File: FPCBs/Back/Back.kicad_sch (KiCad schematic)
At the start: 24 parts, among them J1 To PCB, J2 To Front, J3 Front, J4 EVF_SENSOR, J5 From LCD, SW1 MENU/SET, SW10 -+-, SW11 PLAY, SW12 BACK_WHEEL, SW13 S/C/M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

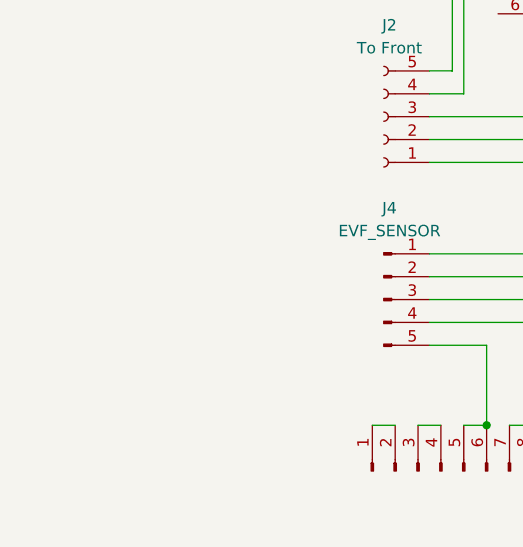
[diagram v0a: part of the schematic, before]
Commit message: Update the licence with CERN-OHL-P-2.0
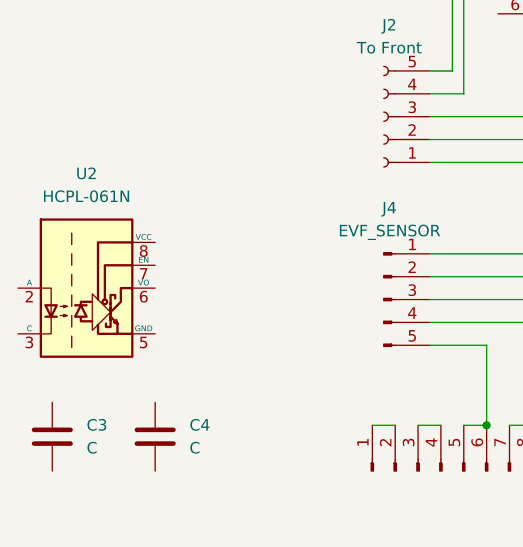
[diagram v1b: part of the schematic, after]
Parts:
- added C3, C4: C, Leica-G9ii:R_0603, symbol Device:C
- added U2: HCPL-061N, Package_SO:SOIC-8_3.9x4.9mm_P1.27mm, symbol Isolator:HCPL-061N
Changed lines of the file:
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@@
+	)
+	(symbol
+		(lib_id "Isolator:HCPL-061N")
+		(at 44.45 139.7 0)
+		(unit 1)
+		(exclude_from_sim no)
+		(in_bom yes)
+		(on_board yes)
+		(dnp no)
+		(fields_autoplaced yes)
+		(property "Reference" "U2"
+			(at 44.45 127 0)
+			(effects
+				(font
+					(size 1.27 1.27)
+				)
+			)
+		)
+		(property "Value" "HCPL-061N"
+			(at 44.45 129.54 0)
+			(effects
+				(font
+					(size 1.27 1.27)
+				)
+			)
+		)
+		(property "Footprint" "Package_SO:SOIC-8_3.9x4.9mm_P1.27mm"
+			(at 44.45 152.4 0)
+			(effects
+				(font
+					(size 1.27 1.27)
+				)
+				(hide yes)
+			)
+		)
+		(property "Datasheet" "http://docs.avagotech.com/docs/AV02-0391EN"
+			(at 22.86 124.46 0)
+			(effects
+				(font
+					(size 1.27 1.27)
+				)
+				(hide yes)
+			)
+		)
+		(property "Description" "Single High Speed HCMOS/LSTTL/TTL Compatible Optocoupler with enable, dV/dt 1000/us, VCM 1000, -0.5V to 7V VCC, SOIC-8"
+			(at 44.45 139.7 0)
+			(effects
+				(font
+					(size 1.27 1.27)
+				)
+				(hide yes)
+			)
+		)
+		(pin "5"
+		)
+		(pin "6"
+		)
+		(pin "8"
+		)
+		(pin "2"
+		)
+		(pin "3"
+		)
+		(pin "1"
+		)
+		(pin "7"
+		)
+		(instances
+			(project ""
+				(path "/2c10aa51-a3b8-43c6-b36e-0de96e4fe4d6"
+					(reference "U2")
+					(unit 1)
+				)
+			)
+		)
 	)
 	(symbol
@@
 	)
 	(symbol
+		(lib_id "Device:C")
+		(at 40.64 156.21 0)
+		(unit 1)
+		(exclude_from_sim no)
+		(in_bom yes)
+		(on_board yes)
+		(dnp no)
+		(fields_autoplaced yes)
+		(property "Reference" "C3"
+			(at 44.45 154.9399 0)
+			(effects
+				(font
+					(size 1.27 1.27)
+				)
+				(justify left)
+			)
+		)
+		(property "Value" "C"
+			(at 44.45 157.4799 0)
+			(effects
+				(font
+					(size 1.27 1.27)
+				)
+				(justify left)
+			)
+		)
+		(property "Footprint" "Leica-G9ii:R_0603"
+			(at 41.6052 160.02 0)
+			(effects
+				(font
+					(size 1.27 1.27)
+				)
+				(hide yes)
+			)
+		)
+		(property "Datasheet" "~"
+			(at 40.64 156.21 0)
+			(effects
+				(font
+					(size 1.27 1.27)
+				)
+				(hide yes)
+			)
+		)
+		(property "Description" "Unpolarized capacitor"
+			(at 40.64 156.21 0)
+			(effects
+				(font
+					(size 1.27 1.27)
+				)
+				(hide yes)
+			)
+		)
+		(pin "2"
+		)
+		(pin "1"
+		)
+		(instances
+			(project "Back"
+				(path "/2c10aa51-a3b8-43c6-b36e-0de96e4fe4d6"
+					(reference "C3")
+					(unit 1)
+				)
+			)
+		)
+	)
+	(symbol
 		(lib_id "Switch:SW_Push_Dual_x2")
 		(at 154.94 95.25 0)
@@
 					(unit 1)
 				)
+			)
+		)
+	)
+	(symbol
+		(lib_id "Device:C")
+		(at 52.07 156.21 0)
+		(unit 1)
+		(exclude_from_sim no)
+		(in_bom yes)
+		(on_board yes)
+		(dnp no)
+		(fields_autoplaced yes)
+		(property "Reference" "C4"
+			(at 55.88 154.9399 0)
+			(effects
+				(font
+					(size 1.27 1.27)
+				)
+				(justify left)
+			)
+		)
+		(property "Value" "C"
+			(at 55.88 157.4799 0)
+			(effects
+				(font
+					(size 1.27 1.27)
+				)
+				(justify left)
+			)
+		)
+		(property "Footprint" "Leica-G9ii:R_0603"
+			(at 53.0352 160.02 0)
+			(effects
+				(font
+					(size 1.27 1.27)
+				)
+				(hide yes)
+			)
+		)
+		(property "Datasheet" "~"
+			(at 52.07 156.21 0)
+			(effects
+				(font
+					(size 1.27 1.27)
+				)
+				(hide yes)
+			)
+		)
+		(property "Description" "Unpolarized capacitor"
+			(at 52.07 156.21 0)
+			(effects
+				(font
+					(size 1.27 1.27)
+				)
+				(hide yes)
+			)
+		)
+		(pin "2"
+		)
+		(pin "1"
+		)
+		(instances
+			(project "Back"
+				(path "/2c10aa51-a3b8-43c6-b36e-0de96e4fe4d6"
+					(reference "C4")
+					(unit 1)
+				)

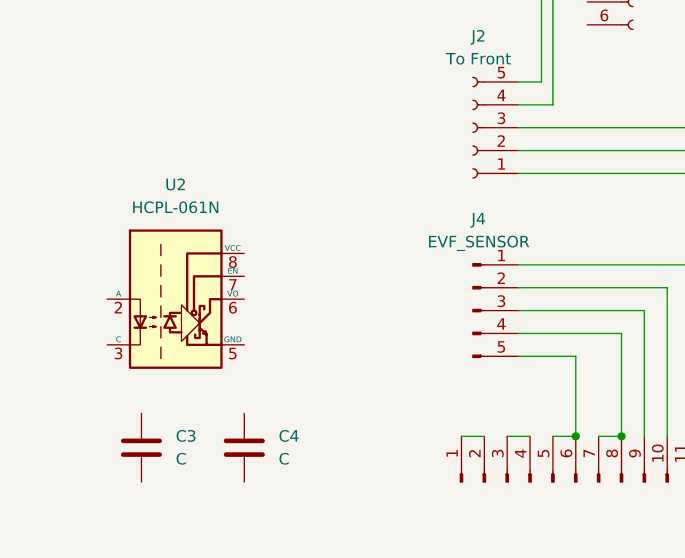
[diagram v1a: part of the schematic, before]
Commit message: Add EVF optocoupler
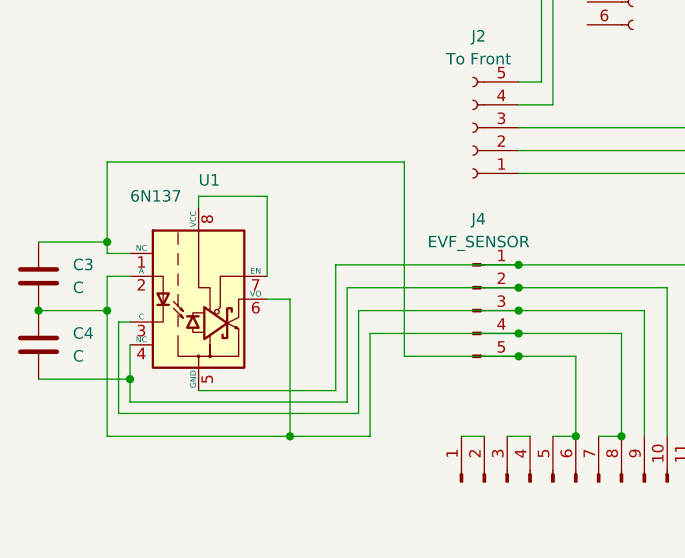
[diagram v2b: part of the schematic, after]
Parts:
- removed U2: HCPL-061N, Package_SO:SOIC-8_3.9x4.9mm_P1.27mm, symbol Isolator:HCPL-061N
- added U1: 6N137, Leica-G9ii:Optocoupler_EVF, symbol Isolator:6N137
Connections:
- net at C3.1: now also J1.5 (Pin_5), J1.6 (Pin_6), J4.5 (Pin_5), U1.1 (NC)
- net at C3.2: now also C4.1, J1.7 (Pin_7), J1.8 (Pin_8), J4.4 (Pin_4), U1.2 (A), U1.6 (VO)
- net at J1.10 (Pin_10), J4.2 (Pin_2): now also C4.2, U1.4 (NC)
- net at J1.11 (Pin_11), J4.1 (Pin_1): now also U1.5 (GND)
- net at J1.9 (Pin_9), J4.3 (Pin_3): now also U1.3 (C)
- new net: U1.7 (EN), U1.8 (VCC)
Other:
- moved on the sheet: C3, C4

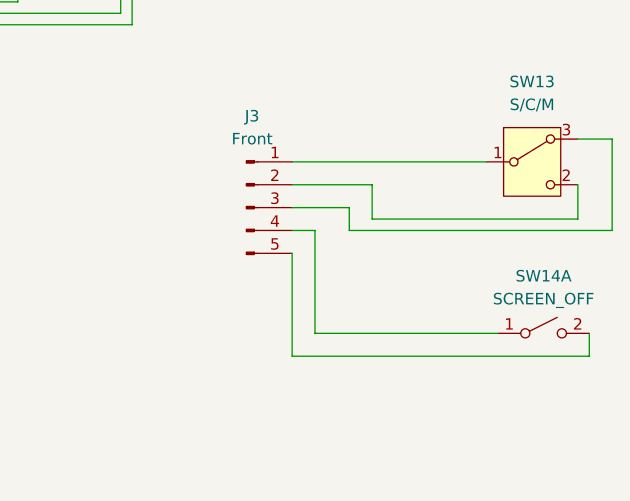
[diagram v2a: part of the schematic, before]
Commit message: Improve the back fpcb
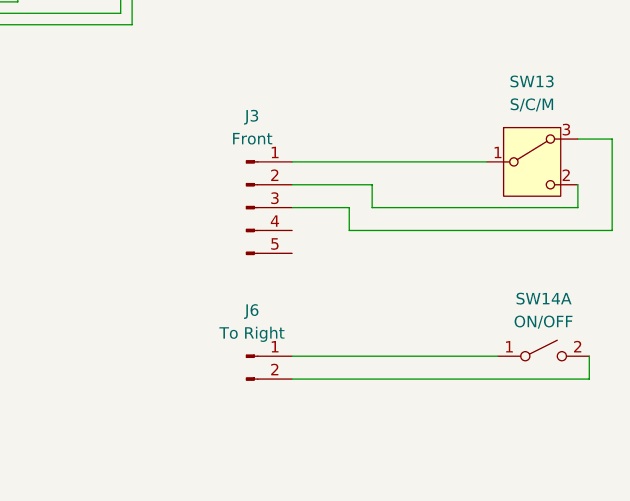
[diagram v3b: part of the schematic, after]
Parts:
- added J6: To Right, Leica-G9ii:Connector-Screw-2Pins, symbol Connector:Conn_01x02_Pin
- SW14: value SCREEN_OFF -> ON/OFF
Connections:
- net at SW14.1 (A): now also J6.1 (Pin_1); no longer J3.4 (Pin_4)
- net at SW14.2 (B): now also J6.2 (Pin_2); no longer J3.5 (Pin_5)
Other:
- moved on the sheet: SW14A
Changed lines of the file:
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@@
-	(wire
-		(pts
-			(xy 256.54 149.86) (xy 236.22 149.86)
-		)
-		(stroke
-			(width 0)
-			(type default)
-		)
-	)
 	(wire
 		(pts
@@
 	(wire
 		(pts
-			(xy 242.57 137.16) (xy 265.43 137.16)
+			(xy 242.57 135.89) (xy 265.43 135.89)
 		)
 		(stroke
@@
 	(wire
 		(pts
-			(xy 236.22 138.43) (xy 233.68 138.43)
-		)
-		(stroke
-			(width 0)
-			(type default)
-		)
-	)
-	(wire
-		(pts
 			(xy 81.28 154.94) (xy 83.82 154.94)
 		)
@@
 	(wire
 		(pts
-			(xy 233.68 140.97) (xy 233.68 152.4)
-		)
-		(stroke
-			(width 0)
-			(type default)
-		)
-	)
-	(wire
-		(pts
 			(xy 111.76 120.65) (xy 111.76 154.94)
 		)
@@
 	(wire
 		(pts
-			(xy 266.7 152.4) (xy 266.7 149.86)
+			(xy 266.7 154.94) (xy 266.7 152.4)
 		)
 		(stroke
@@
 	(wire
 		(pts
-			(xy 265.43 137.16) (xy 265.43 133.35)
-		)
-		(stroke
-			(width 0)
-			(type default)
-		)
-	)
-	(wire
-		(pts
-			(xy 233.68 152.4) (xy 266.7 152.4)
+			(xy 265.43 135.89) (xy 265.43 133.35)
+		)
+		(stroke
+			(width 0)
+			(type default)
+		)
+	)
+	(wire
+		(pts
+			(xy 233.68 154.94) (xy 266.7 154.94)
 		)
 		(stroke
@@
 	(wire
 		(pts
-			(xy 242.57 133.35) (xy 242.57 137.16)
-		)
-		(stroke
-			(width 0)
-			(type default)
-		)
-	)
-	(wire
-		(pts
-			(xy 236.22 149.86) (xy 236.22 138.43)
+			(xy 242.57 133.35) (xy 242.57 135.89)
 		)
 		(stroke
@@
 		(pts
 			(xy 154.94 113.03) (xy 154.94 154.94)
+		)
+		(stroke
+			(width 0)
+			(type default)
+		)
+	)
+	(wire
+		(pts
+			(xy 233.68 152.4) (xy 256.54 152.4)
 		)
 		(stroke
@@
 	)
 	(symbol
+		(lib_id "Connector:Conn_01x02_Pin")
+		(at 228.6 152.4 0)
+		(unit 1)
+		(exclude_from_sim no)
+		(in_bom yes)
+		(on_board yes)
+		(dnp no)
+		(fields_autoplaced yes)
+		(property "Reference" "J6"
+			(at 229.235 147.32 0)
+			(effects
+				(font
+					(size 1.27 1.27)
+				)
+			)
+		)
+		(property "Value" "To Right"
+			(at 229.235 149.86 0)
+			(effects
+				(font
+					(size 1.27 1.27)
+				)
+			)
+		)
+		(property "Footprint" "Leica-G9ii:Connector-Screw-2Pins"
+			(at 228.6 152.4 0)
+			(effects
+				(font
+					(size 1.27 1.27)
+				)
+				(hide yes)
+			)
+		)
+		(property "Datasheet" "~"
+			(at 228.6 152.4 0)
+			(effects
+				(font
+					(size 1.27 1.27)
+				)
+				(hide yes)
+			)
+		)
+		(property "Description" "Generic connector, single row, 01x02, script generated"
+			(at 228.6 152.4 0)
+			(effects
+				(font
+					(size 1.27 1.27)
+				)
+				(hide yes)
+			)
+		)
+		(pin "1"
+		)
+		(pin "2"
+		)
+		(instances
+			(project ""
+				(path "/2c10aa51-a3b8-43c6-b36e-0de96e4fe4d6"
+					(reference "J6")
+					(unit 1)
+				)
+			)
+		)
+	)
+	(symbol
 		(lib_id "Device:C")
 		(at 29.21 137.16 0)
@@
 	(symbol
 		(lib_id "Switch:SW_DPST_x2")
-		(at 261.62 149.86 0)
+		(at 261.62 152.4 0)
 		(unit 1)
 		(exclude_from_sim no)
@@
 		(fields_autoplaced yes)
 		(property "Reference" "SW14"
-			(at 261.62 143.51 0)
-			(effects
-				(font
-					(size 1.27 1.27)
-				)
-			)
-		)
-		(property "Value" "SCREEN_OFF"
 			(at 261.62 146.05 0)
 			(effects
@@
 			)
 		)
+		(property "Value" "ON/OFF"
+			(at 261.62 148.59 0)
+			(effects
+				(font
+					(size 1.27 1.27)
+				)
+			)
+		)
 		(property "Footprint" "Leica-G9ii:Switch_Detection"
-			(at 261.62 149.86 0)
+			(at 261.62 152.4 0)
 			(effects
 				(font
@@
 		)
 		(property "Datasheet" "~"
-			(at 261.62 149.86 0)
+			(at 261.62 152.4 0)
 			(effects
 				(font
@@
 		)
 		(property "Description" "Single Pole Single Throw (SPST) switch, separate symbol"
-			(at 261.62 149.86 0)
-			(effects
-				(font
+			(at 261.62 152.4 0)
+			(effects
+				(font

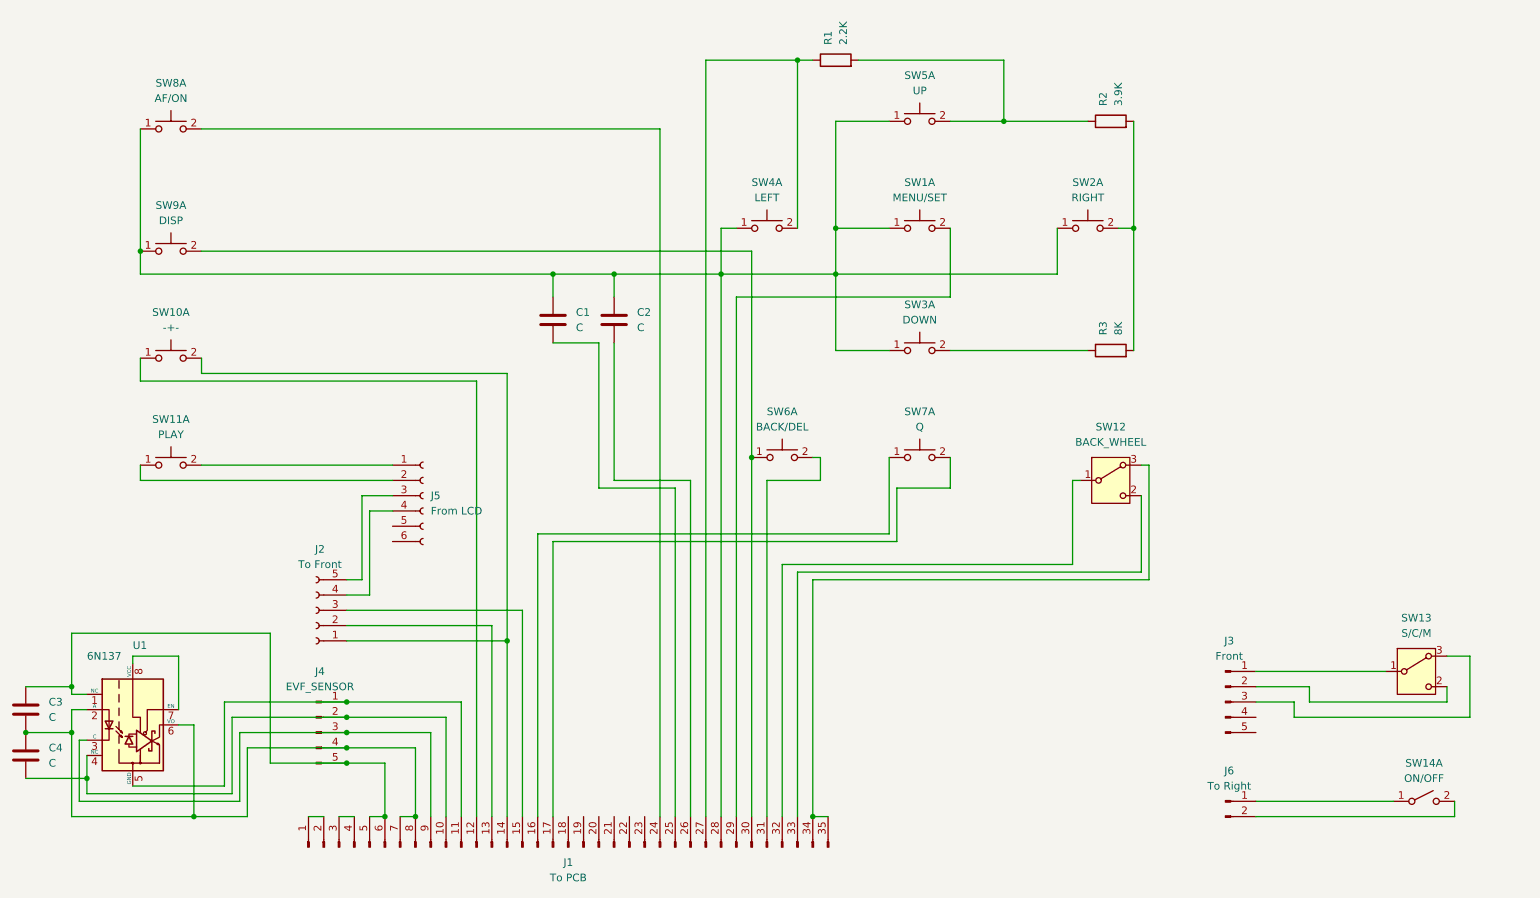
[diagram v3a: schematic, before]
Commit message: Add front lever flex cable
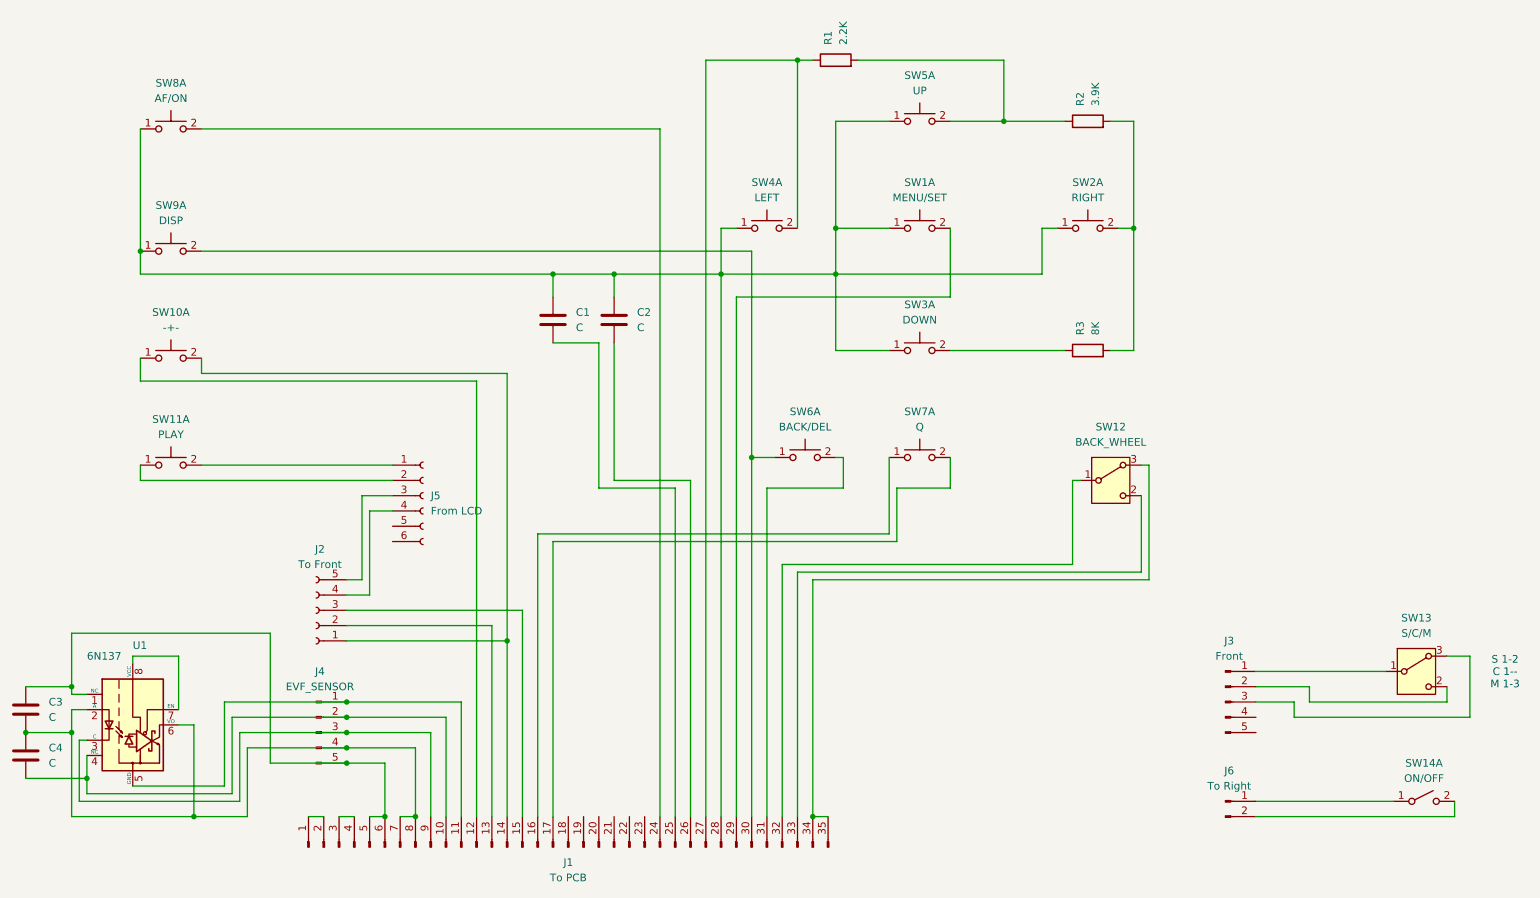
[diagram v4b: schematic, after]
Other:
- note added: "S 1-2 C 1-- M 1-3"
- moved on the sheet: R2, R3, SW6A
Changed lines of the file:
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@@
 	(generator_version "9.0")
 	(paper "A4")
+	(text "S 1-2\nC 1--\nM 1-3"
+		(exclude_from_sim no)
+		(at 275.082 131.064 0)
+		(effects
+			(font
+				(size 1.27 1.27)
+			)
+		)
+	)
 	(junction
 		(at 88.9 154.94)
@@
 	)
 	(junction
-		(at 213.36 57.15)
-		(diameter 0)
-		(color 0 0 0 0)
-	)
-	(junction
 		(at 93.98 154.94)
 		(diameter 0)
@@
 	)
 	(junction
+		(at 213.36 57.15)
+		(diameter 0)
+		(color 0 0 0 0)
+	)
+	(junction
 		(at 36.83 140.97)
 		(diameter 0)
@@
 	(wire
 		(pts
+			(xy 153.67 95.25) (xy 149.86 95.25)
+		)
+		(stroke
+			(width 0)
+			(type default)
+		)
+	)
+	(wire
+		(pts
 			(xy 36.83 124.46) (xy 69.85 124.46)
 		)
@@
 	(wire
 		(pts
+			(xy 198.12 57.15) (xy 200.66 57.15)
+		)
+		(stroke
+			(width 0)
+			(type default)
+		)
+	)
+	(wire
+		(pts
 			(xy 144.78 64.77) (xy 144.78 154.94)
 		)
@@
 	(wire
 		(pts
+			(xy 213.36 77.47) (xy 209.55 77.47)
+		)
+		(stroke
+			(width 0)
+			(type default)
+		)
+	)
+	(wire
+		(pts
 			(xy 233.68 133.35) (xy 242.57 133.35)
 		)
@@
 	(wire
 		(pts
-			(xy 152.4 99.06) (xy 161.29 99.06)
+			(xy 152.4 100.33) (xy 165.1 100.33)
 		)
 		(stroke
@@
 	(wire
 		(pts
-			(xy 161.29 95.25) (xy 161.29 99.06)
+			(xy 165.1 95.25) (xy 165.1 100.33)
 		)
 		(stroke
@@
 	(wire
 		(pts
-			(xy 200.66 57.15) (xy 200.66 64.77)
+			(xy 198.12 57.15) (xy 198.12 64.77)
 		)
 		(stroke
@@
 	(wire
 		(pts
-			(xy 160.02 95.25) (xy 161.29 95.25)
+			(xy 163.83 95.25) (xy 165.1 95.25)
 		)
 		(stroke
@@
 	(wire
 		(pts
-			(xy 191.77 39.37) (xy 205.74 39.37)
+			(xy 191.77 39.37) (xy 201.93 39.37)
 		)
 		(stroke
@@
 	(wire
 		(pts
-			(xy 210.82 57.15) (xy 213.36 57.15)
+			(xy 213.36 57.15) (xy 210.82 57.15)
 		)
 		(stroke
@@
 	(wire
 		(pts
-			(xy 200.66 64.77) (xy 163.83 64.77)
+			(xy 198.12 64.77) (xy 163.83 64.77)
 		)
 		(stroke
@@
 	(wire
 		(pts
-			(xy 182.88 77.47) (xy 205.74 77.47)
+			(xy 182.88 77.47) (xy 201.93 77.47)
+		)
+		(stroke
+			(width 0)
+			(type default)
+		)
+	)
+	(wire
+		(pts
+			(xy 213.36 39.37) (xy 209.55 39.37)
 		)
 		(stroke
@@
 	(wire
 		(pts
-			(xy 152.4 99.06) (xy 152.4 154.94)
+			(xy 152.4 100.33) (xy 152.4 154.94)
 		)
 		(stroke
@@
 	(symbol
 		(lib_id "Device:R")
-		(at 209.55 39.37 90)
+		(at 205.74 39.37 90)
 		(unit 1)
 		(exclude_from_sim no)
@@
 		(fields_autoplaced yes)
 		(property "Reference" "R2"
-			(at 208.2799 36.83 0)
+			(at 204.4699 36.83 0)
 			(effects
 				(font
@@
 		)
 		(property "Value" "3.9K"
-			(at 210.8199 36.83 0)
+			(at 207.0099 36.83 0)
 			(effects
 				(font
@@
 		)
 		(property "Footprint" "Leica-G9ii:R_0603"
-			(at 209.55 41.148 90)
+			(at 205.74 41.148 90)
 			(effects
 				(font
@@
 		)
 		(property "Datasheet" "~"
-			(at 209.55 39.37 0)
+			(at 205.74 39.37 0)
 			(effects
 				(font
@@
 		)
 		(property "Description" "Resistor"
-			(at 209.55 39.37 0)
+			(at 205.74 39.37 0)
 			(effects
 				(font
@@
 	(symbol
 		(lib_id "Switch:SW_Push_Dual_x2")
-		(at 154.94 95.25 0)
+		(at 158.75 95.25 0)
 		(unit 1)
 		(exclude_from_sim no)
@@
 		(fields_autoplaced yes)
 		(property "Reference" "SW6"
-			(at 154.94 87.63 0)
+			(at 158.75 87.63 0)
 			(effects
 				(font
@@
 		)
 		(property "Value" "BACK/DEL"
-			(at 154.94 90.17 0)
+			(at 158.75 90.17 0)
 			(effects
 				(font
@@
 		)
 		(property "Footprint" "Leica-G9ii:Push_Button"
-			(at 154.94 90.17 0)
+			(at 158.75 90.17 0)
 			(effects
 				(font
@@
 		)
 		(property "Datasheet" "~"
-			(at 154.94 90.17 0)
+			(at 158.75 90.17 0)
 			(effects
 				(font
@@
 		)
 		(property "Description" "Push button switch, generic, separate symbols, four pins"
-			(at 154.94 95.25 0)
+			(at 158.75 95.25 0)
 			(effects
 				(font
@@
 	(symbol
 		(lib_id "Device:R")
-		(at 209.55 77.47 90)
+		(at 205.74 77.47 90)
 		(unit 1)
 		(exclude_from_sim no)
@@
 		(fields_autoplaced yes)
 		(property "Reference" "R3"
-			(at 208.2799 74.93 0)
+			(at 204.4699 74.93 0)
 			(effects
 				(font
@@
 		)
 		(property "Value" "8K"
-			(at 210.8199 74.93 0)
+			(at 207.0099 74.93 0)
 			(effects
 				(font
@@
 		)
 		(property "Footprint" "Leica-G9ii:R_0603"
-			(at 209.55 79.248 90)
+			(at 205.74 79.248 90)
 			(effects
 				(font
@@
 		)
 		(property "Datasheet" "~"
-			(at 209.55 77.47 0)
+			(at 205.74 77.47 0)
 			(effects
 				(font
@@
 		)
 		(property "Description" "Resistor"
-			(at 209.55 77.47 0)
+			(at 205.74 77.47 0)
 			(effects
 				(font
